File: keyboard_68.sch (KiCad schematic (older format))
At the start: 19 parts, among them J1 Conn_01x02_Male, J70 Conn_02x03_Odd_Even, SW1 EVQPUJ02K / EVQPUA02K, U1 USB_C, U2 nRF52840_som

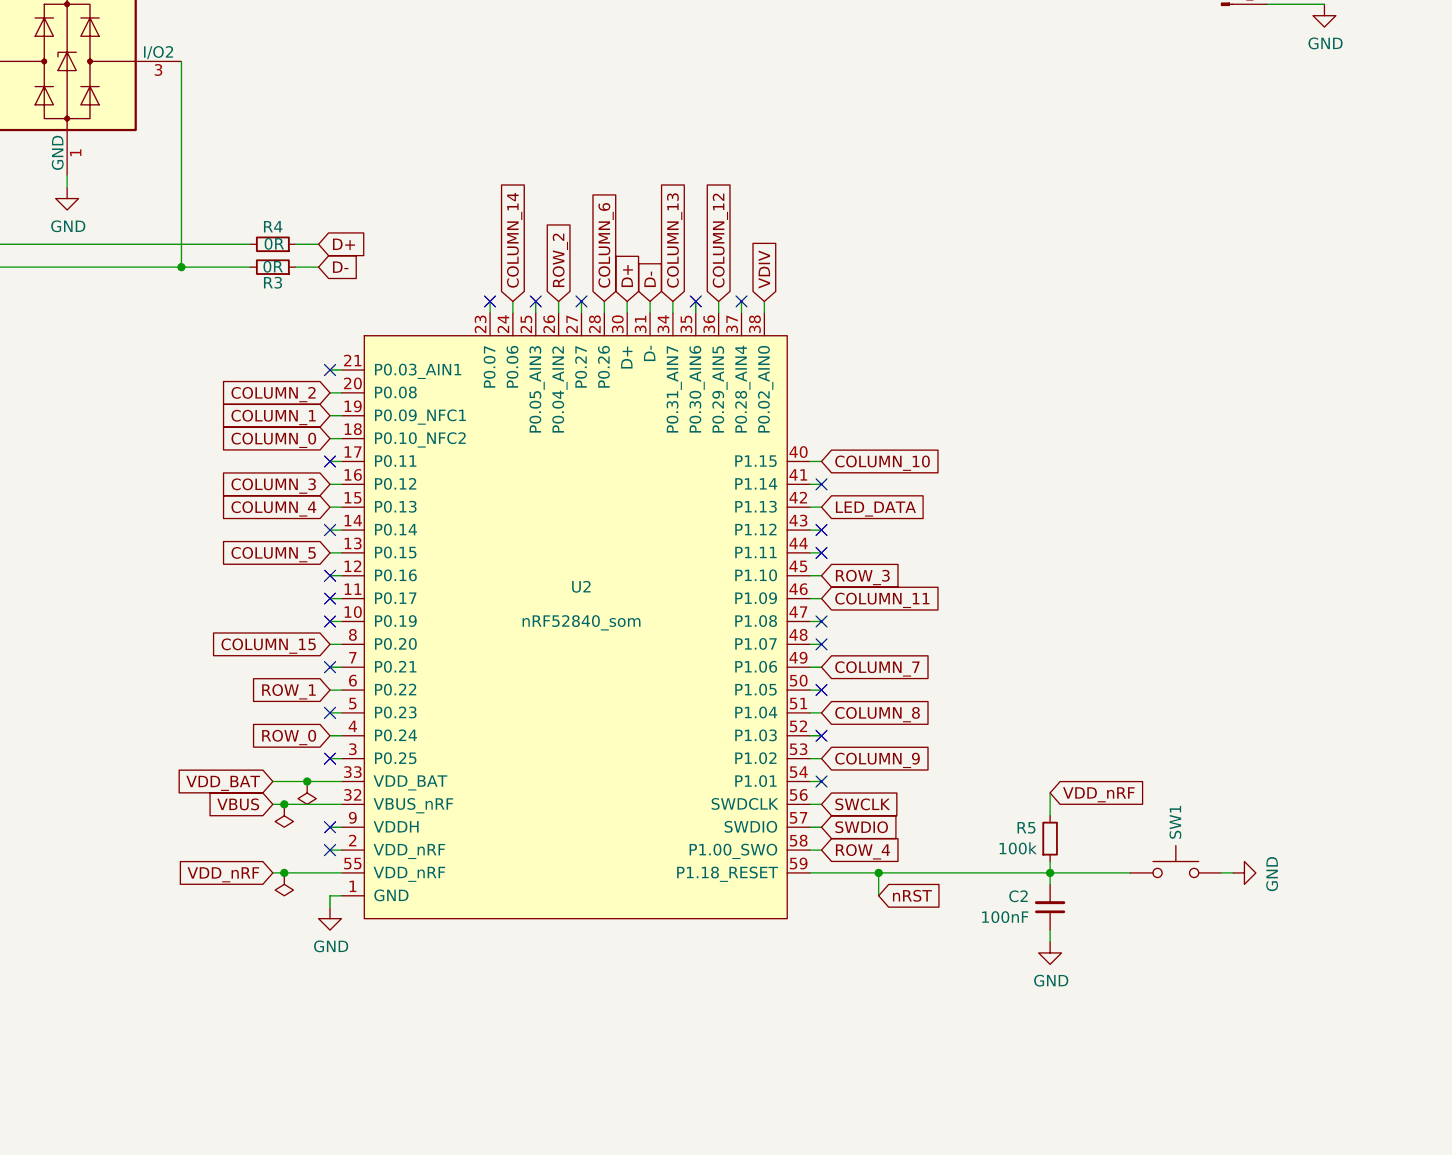
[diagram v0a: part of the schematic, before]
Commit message: place all components on backside
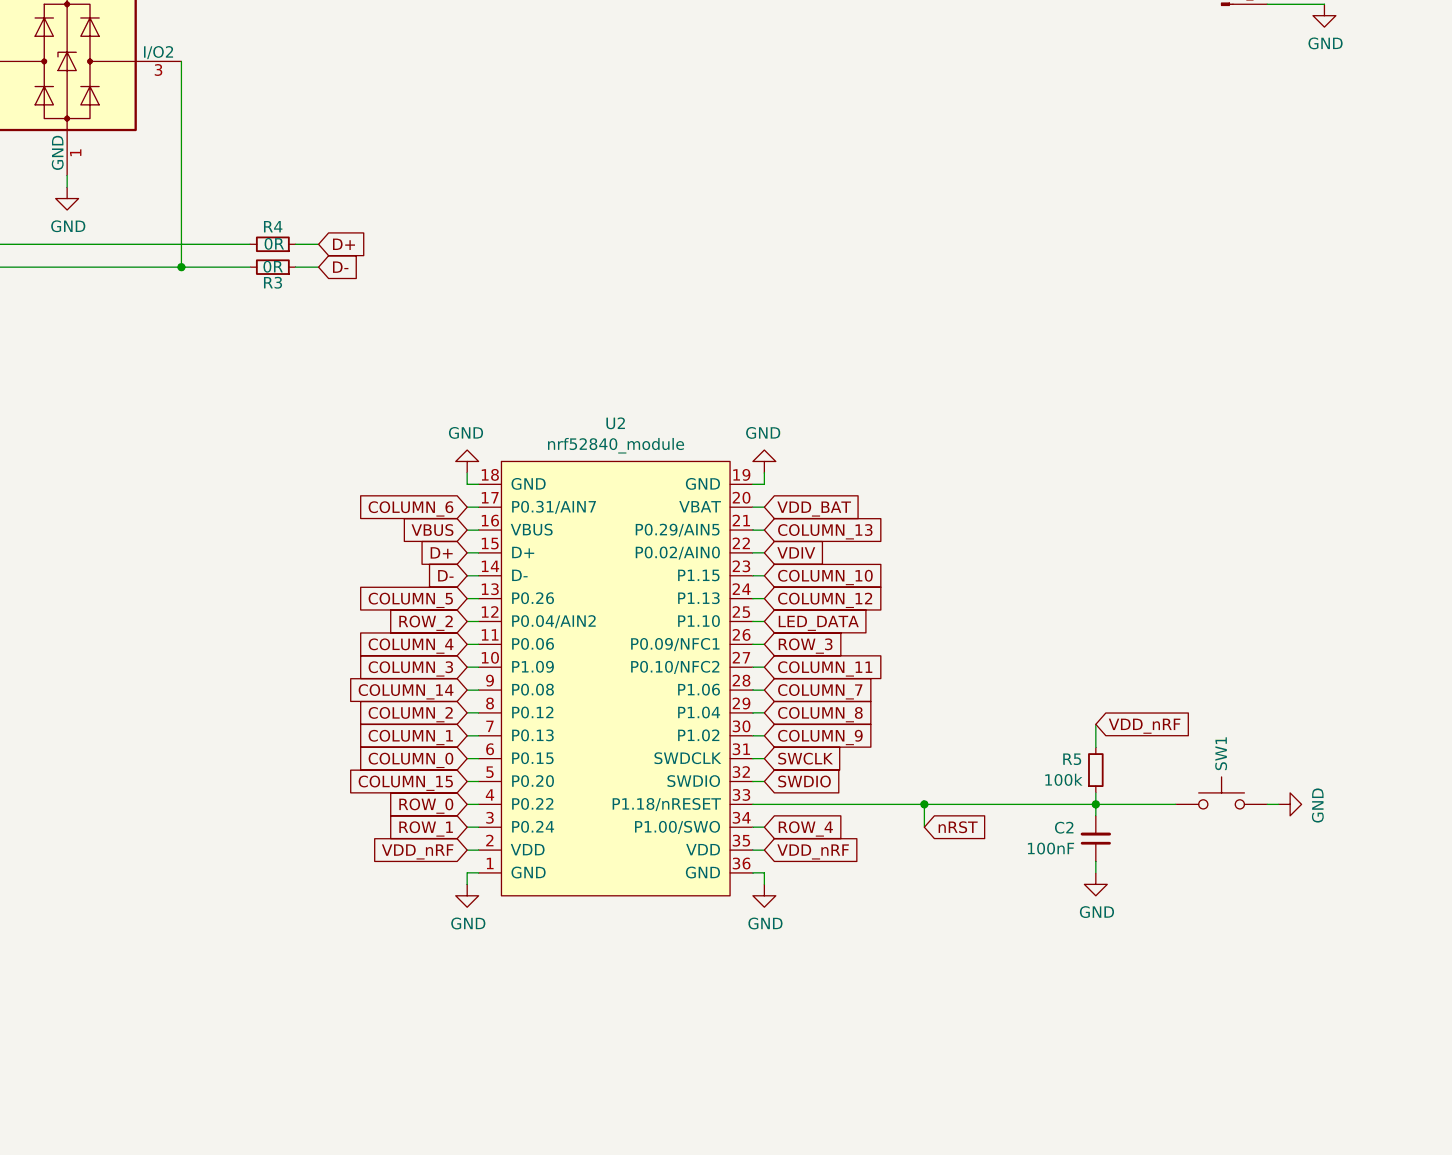
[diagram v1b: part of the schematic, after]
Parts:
- removed U2: nRF52840_som, nrf52840_som:nrf52840_som, symbol nRF52840_som:nRF52840_som
- added U2: nrf52840_module, custom_footprints:nrf52840_module, symbol nRF52840_module:nrf52840_module
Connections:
- net COLUMN_0: now also U2.6 (P0.15)
- net COLUMN_1: now also U2.7 (P0.13)
- net COLUMN_10: now also U2.23 (P1.15)
- net COLUMN_11: now also U2.27 (P0.10/NFC2)
- net COLUMN_12: now also U2.24 (P1.13)
- net COLUMN_13: now also U2.21 (P0.29/AIN5)
- net COLUMN_14: now also U2.9 (P0.08)
- net COLUMN_15: now also U2.5 (P0.20)
- net COLUMN_2: now also U2.8 (P0.12)
- net COLUMN_3: now also U2.10 (P1.09)
- net COLUMN_4: now also U2.11 (P0.06)
- net COLUMN_5: now also U2.13 (P0.26)
- net COLUMN_6: now also U2.17 (P0.31/AIN7)
- net COLUMN_7: now also U2.28 (P1.06)
- net COLUMN_8: now also U2.29 (P1.04)
- net COLUMN_9: now also U2.30 (P1.02)
- net D+: now also U2.15 (D+)
- net D-: now also U2.14 (D-)
- net GND: now also U2.1 (GND), U2.18 (GND), U2.19 (GND), U2.36 (GND)
- net LED_DATA: now also U2.25 (P1.10)
- net ROW_0: now also U2.4 (P0.22)
- net ROW_1: now also U2.3 (P0.24)
- net ROW_2: now also U2.12 (P0.04/AIN2)
- net ROW_3: now also U2.26 (P0.09/NFC1)
- net ROW_4: now also U2.34 (P1.00/SWO)
- net SWCLK: now also U2.31 (SWDCLK)
- net SWDIO: now also U2.32 (SWDIO)
- net VBUS: now also U2.16 (VBUS)
- net VDD_BAT: now also U2.20 (VBAT)
- net VDD_nRF: now also U2.2 (VDD), U2.35 (VDD)
- net VDIV: now also U2.22 (P0.02/AIN0)
- net nRST: now also U2.33 (P1.18/nRESET)
- no-connect marks 35 -> 11
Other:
- moved on the sheet: C2, R5, SW1
